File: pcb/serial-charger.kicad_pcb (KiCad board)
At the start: 2 copper layers, 87 x 21 mm, 67 parts, among them IC201 MCU-ATMEGA328P-MU_QFN32_, J202 jumper, P102 CONN_01X02, P103 CONN_01X04, P201 CONNECTOR, P202 CONNECTOR, P203 CONNECTOR, P204 CONNECTOR, P205 CONNECTOR, P206 CONNECTOR, P207 CONNECTOR, P208 CONNECTOR, P209 CONNECTOR, P210 CONNECTOR, P211 CONNECTOR, P212 CONNECTOR, P213 CONNECTOR, P214 CONNECTOR, P215 CONNECTOR, P216 CONNECTOR, P217 CONNECTOR, P218 CONNECTOR, P219 CONNECTOR, P220 CONNECTOR, P221 CONNECTOR, P222 CONN_01X03, P223 CONNECTOR, P224 CONNECTOR, Q201 SMD-MOSFET-P-CH-8V-4.1A-CJ230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, U301 PMIC-CN3065_DFN8_, U302 PMIC-ISL97516IUZ-TK_MSOP8_, U401 INTERFACE-CH340T_SSOP20_, Y401 SMD-CRYSTAL-12MHZ-20PF-20PPM-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, x201 SMD-CRYSTAL-16MHZ-8PF-20PPM-4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

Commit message: layout mostly done
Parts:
- removed REF**: via, netl:via
- added JP11: CONN_01X01, netl:1Pin_through, F.Cu at (137.3, 92.4)
- added JP11: CONN_01X01, netl:1Pin_through, F.Cu at (139.8, 92.4)
- added JP11: CONN_01X01, netl:1Pin_through, F.Cu at (144.9, 92.4)
- added JP11: CONN_01X01, netl:1Pin_through, F.Cu at (167.8, 92.4)
- added JP11: CONN_01X01, netl:1Pin_through, F.Cu at (144.9, 107.6)
- added JP11: CONN_01X01, netl:1Pin_through, F.Cu at (170.3, 92.4)
- added P213: CONNECTOR, netl:1Pin_through, F.Cu at (142.4, 92.4)
- C201, C202, C203, C204, C205, C301, C302, C303, C304, C305, C401, C402, C403, C404: footprint SeeedOPL-Capacitor-2016:C0603 -> netl:C0603
- C306, C307: footprint SeeedOPL-Capacitor-2016:C0805 -> netl:C0805
- P201, P202, P203, P204, P205, P206, P207, P208, P209, P210, P211, P212, P213, P214, P215, P216, P217, P218, P219, P220, P221, P223, P224: footprint netl:1Pin_small -> netl:1Pin_through
- R304: footprint Resistors_SMD:R_0603 -> SeeedOPL-Resistor-2016:R0603
- moved R301 54.1 mm to (110.8, 91.2)
- moved U301 53.8 mm to (116.8, 92.8), turned to 180 degrees
- moved C302 52.4 mm to (114.0, 95.8), turned to 90 degrees
- moved C301 52.2 mm to (114.0, 92.8), turned to 180 degrees
- moved R302 51.9 mm to (110.8, 92.8), turned to 90 degrees
- moved R303 50.9 mm to (110.8, 94.2), turned to 90 degrees
- moved C307 50.3 mm to (120.3, 77.6)
- moved C304 47.9 mm to (137.6, 81.3), turned to 270 degrees
- moved D302 46.7 mm to (124.8, 77.6), turned to 180 degrees
- moved R308 45.6 mm to (127.3, 82.1), turned to 90 degrees
- moved C303 45.4 mm to (125.1, 81.3), turned to 180 degrees
- moved C306 44.4 mm to (140.1, 77.3), turned to 270 degrees
- moved R304 44.1 mm to (117.0, 95.8), turned to 270 degrees
- moved R307 41.2 mm to (127.3, 83.6), turned to 270 degrees
- moved Y401 40.8 mm to (125.5, 105.5), turned to 90 degrees
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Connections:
- C303 pad 1: (no net) -> GND
- C303 pad 2: (no net) -> Net-(C303-Pad2)
- IC201 pad 20: /5V -> Net-(IC201-Pad20)
- R306 pad 1: Net-(C303-Pad~) -> Net-(C303-Pad2)
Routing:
- net /V_USB: track 0.00 -> 40.7 mm
- net GND: track 0.00 -> 17.4 mm, vias 0 -> 9
- net /D+: track 0.00 -> 12.3 mm
- net /D-: track 0.00 -> 12.3 mm
- net Net-(R301-Pad1): track 0.00 -> 9.50 mm
- net Net-(R303-Pad2): track 0.00 -> 9.34 mm
- net Net-(D101-Pad-): track 0.00 -> 7.49 mm
- net /~chrg: track 0.00 -> 4.89 mm
- net /V_BAT: track 0.00 -> 3.16 mm
- net Net-(R304-Pad1): track 0.00 -> 1.70 mm
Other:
- board text removed: "5V"
- board text removed: "GND"
- board text removed: "PORT B"
- board text removed: "PORT C"
- board text removed: "PORT D"

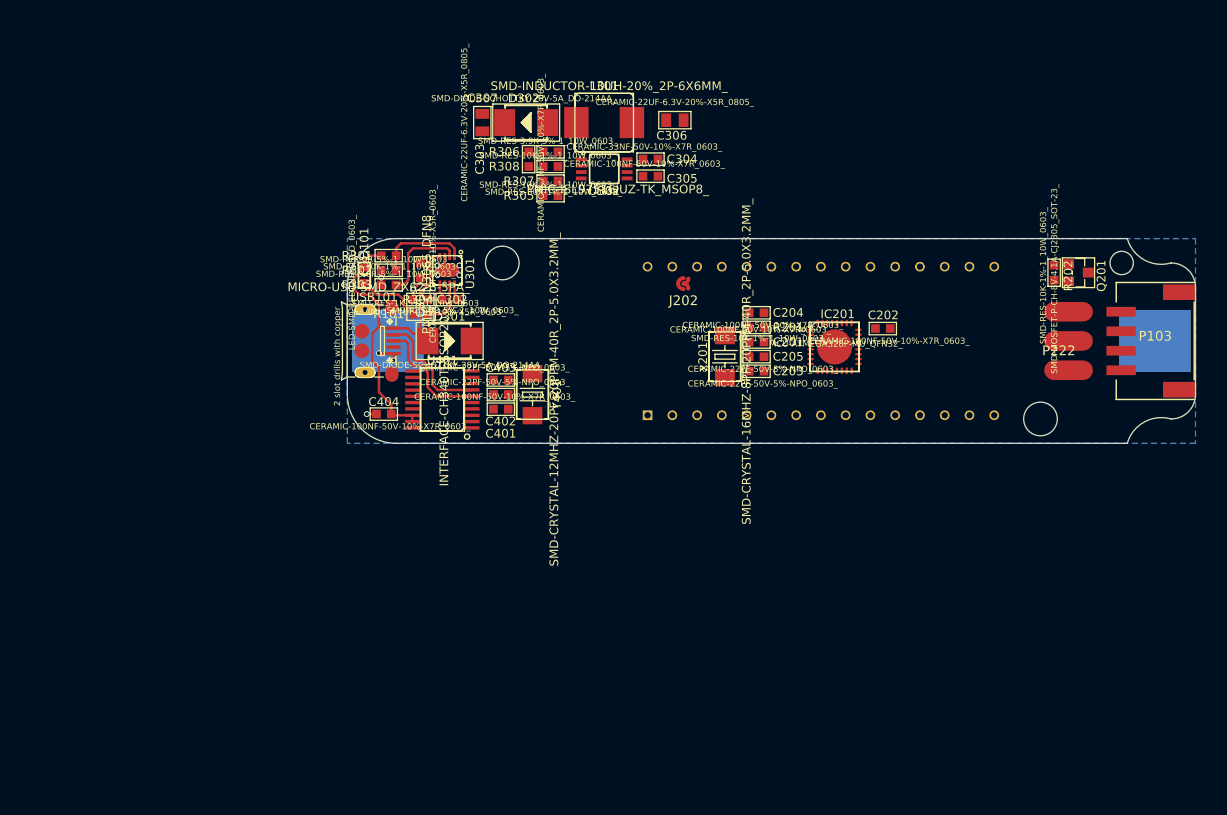
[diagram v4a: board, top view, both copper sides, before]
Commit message: boost circuit layout mostly done
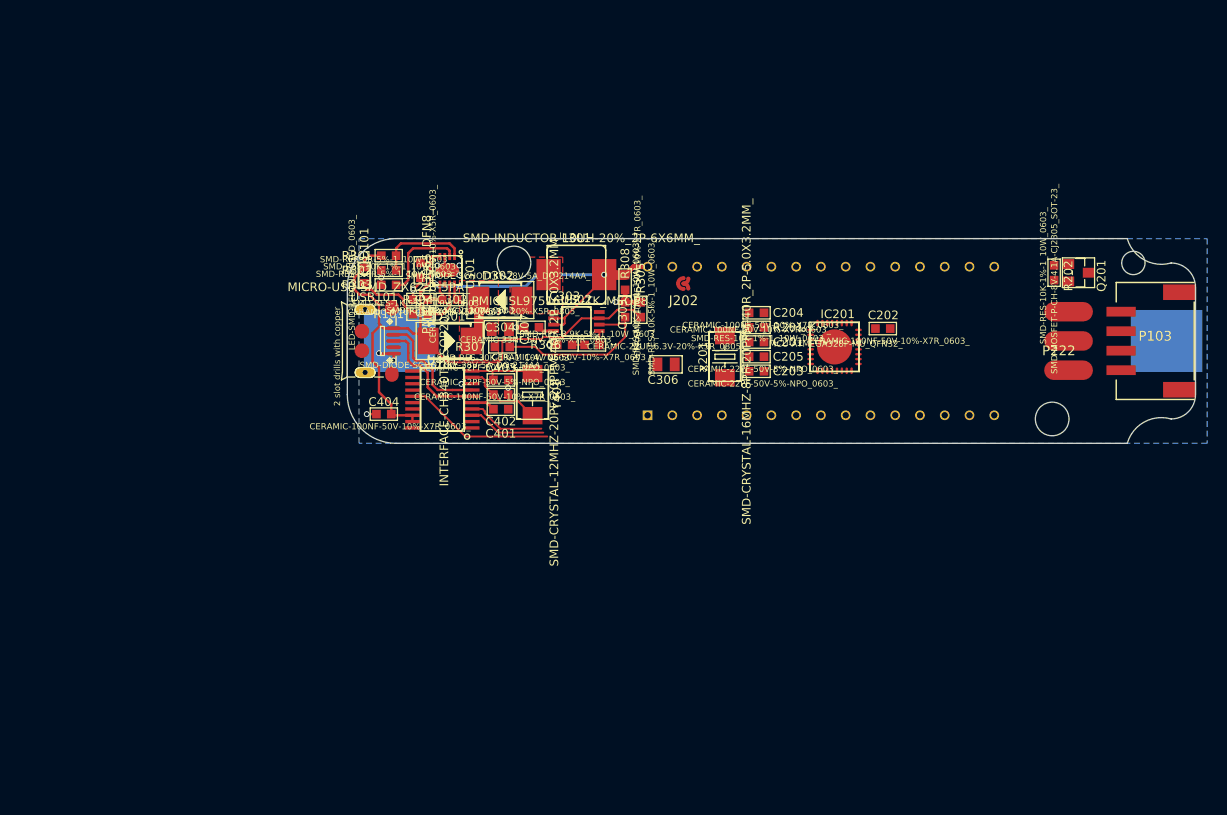
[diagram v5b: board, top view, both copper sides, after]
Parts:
- moved C306 25.1 mm to (139.2, 102.4)
- moved C307 21.3 mm to (122.2, 98.8), turned to 270 degrees
- moved C304 21.1 mm to (125.4, 98.6), turned to 90 degrees
- moved R306 20.3 mm to (131.6, 100.4)
- moved C303 19.4 mm to (128.8, 100.4), turned to 90 degrees
- moved D302 18.4 mm to (122.2, 95.8)
- moved R307 17.7 mm to (122.4, 100.6)
- moved R308 16.6 mm to (135.0, 96.8), turned to 0 degrees
- moved U302 15.9 mm to (130.0, 98.0), turned to 180 degrees
- moved L301 15.9 mm to (130.0, 93.2)
- moved R305 14.9 mm to (136.6, 96.8), turned to 0 degrees
- moved C305 11.2 mm to (135.0, 94.0), turned to 180 degrees
- moved P102 1.20 mm to (151.2, 100.0)
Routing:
- net /V_BAT: track 3.16 -> 36.2 mm, vias 0 -> 2
- net /V_USB: track 40.7 -> 67.2 mm
- net Net-(R307-Pad1): track 0.00 -> 17.7 mm
- net /~DTR: track 0.00 -> 15.5 mm
- net GND: track 17.4 -> 25.6 mm, vias 9 -> 14
- net Net-(C402-Pad2): track 0.00 -> 8.17 mm
- net /RX: track 0.00 -> 8.04 mm
- net /TX: track 0.00 -> 8.02 mm
- net Net-(C403-Pad2): track 0.00 -> 7.26 mm
- net /5V: track 0.00 -> 4.52 mm
- net /3V3: track 0.00 -> 2.46 mm
- net Net-(C304-Pad2): track 0.00 -> 1.64 mm
- net Net-(R306-Pad2): track 0.00 -> 1.43 mm
- net Net-(C303-Pad2): track 0.00 -> 1.28 mm
- added copper zone on F.Cu, net /5V
- added copper zone on F.Cu, net Net-(D302-Pad+)

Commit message: added button, capacitor to led strip power and jumpers to external rx/tx. everything layed out and connected
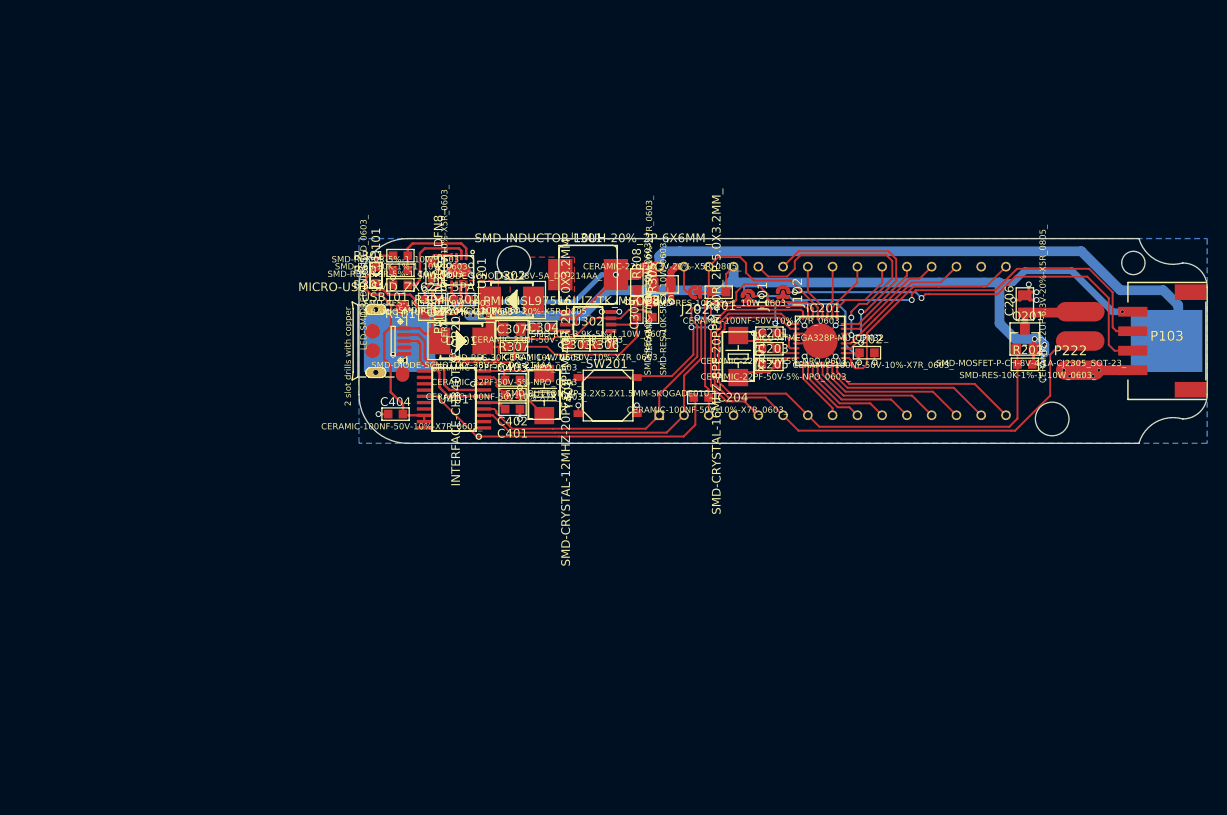
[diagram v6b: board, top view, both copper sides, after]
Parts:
- added C206: CERAMIC-22UF-6.3V-20%-X5R_0805_, netl:C0805, F.Cu at (176.0, 96.2)
- added J101: jumper, netl:Jumper, F.Cu at (147.6, 95.4)
- added J102: jumper, netl:Jumper, F.Cu at (151.2, 95.0)
- added REF**: via, netl:via, F.Cu at (120.6, 97.4)
- added REF**: via, netl:via, F.Cu at (183.0, 103.6)
- added REF**: via, netl:via, F.Cu at (180.6, 102.4)
- added REF**: via, netl:via, F.Cu at (180.6, 103.6)
- added REF**: via, netl:via, F.Cu at (180.0, 103.0)
- added REF**: via, netl:via, F.Cu at (120.0, 97.4)
- added REF**: via, netl:via, F.Cu at (119.4, 97.4)
- added REF**: via, netl:via, F.Cu at (118.8, 97.4)
- added REF**: via, netl:via, F.Cu at (186.0, 97.0)
- added REF**: via, netl:via, F.Cu at (181.8, 102.4)
- added REF**: via, netl:via, F.Cu at (181.8, 103.6)
- added REF**: via, netl:via, F.Cu at (183.6, 103.0)
- added REF**: via, netl:via, F.Cu at (183.0, 102.4)
- added SW201: SMD-BUTTON_4P-5.2X5.2X1.5MM-SKQGADE010_, SeeedOPL-Switch-2016:SW4-SMD-5.2X5.2X1.5MM, F.Cu at (133.2, 105.6)
- moved C204 10.4 mm to (142.8, 105.8)
- moved R202 9.87 mm to (176.0, 102.4), turned to 270 degrees
- moved Q201 8.75 mm to (176.0, 99.8), turned to 0 degrees
- moved C306 8.21 mm to (138.8, 94.2)
- moved R201 5.30 mm to (144.6, 95.0)
- moved C202 2.96 mm to (159.8, 101.2)
- moved C203 2.66 mm to (149.8, 100.8)
- moved C201 1.60 mm to (149.8, 99.2)
- moved IC201 1.60 mm to (155.0, 100.0)
- moved C205 1.54 mm to (149.8, 102.4)
- moved J202 1.51 mm to (142.2, 95.0)
- moved x201 1.37 mm to (146.6, 101.6), turned to 270 degrees
- moved JP11 1.20 mm to (146.1, 92.4)
- moved JP11 1.20 mm to (146.1, 107.6)
- moved JP11 1.20 mm to (171.5, 92.4)
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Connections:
- P103 pad 2: /TX -> /EXT_TX
- P103 pad 3: /RX -> /EXT_RX
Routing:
- net /5V: track 4.52 -> 131.1 mm, vias 0 -> 6
- net /V_BAT: track 36.2 -> 100.0 mm
- net /avr/LED_DATA: track 0.00 -> 60.9 mm
- net /avr/~LED_ENABLE: track 0.00 -> 54.4 mm
- net GND: track 25.6 -> 76.0 mm, vias 14 -> 31
- net /EXT_RX: track 0.00 -> 47.4 mm, vias 0 -> 2
- net /EXT_TX: track 0.00 -> 44.3 mm, vias 0 -> 2
- net /TX: track 8.02 -> 51.7 mm, vias 0 -> 2
- net /avr/BTN: track 0.00 -> 41.0 mm, vias 0 -> 2
- net /RX: track 8.04 -> 47.8 mm, vias 0 -> 2
- net /avr/~RESET: track 0.00 -> 33.8 mm
- net Net-(IC201-Pad22): track 0.00 -> 26.4 mm, vias 0 -> 2
- net Net-(IC201-Pad19): track 0.00 -> 24.9 mm, vias 0 -> 2
- net /avr/SCK: track 0.00 -> 23.5 mm
- net /avr/MISO: track 0.00 -> 19.9 mm
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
